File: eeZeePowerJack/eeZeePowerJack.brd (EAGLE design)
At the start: 29.2 x 13.7 mm, 10 parts, among them J1 POWER_JACKPTH, U2 LD29150DT

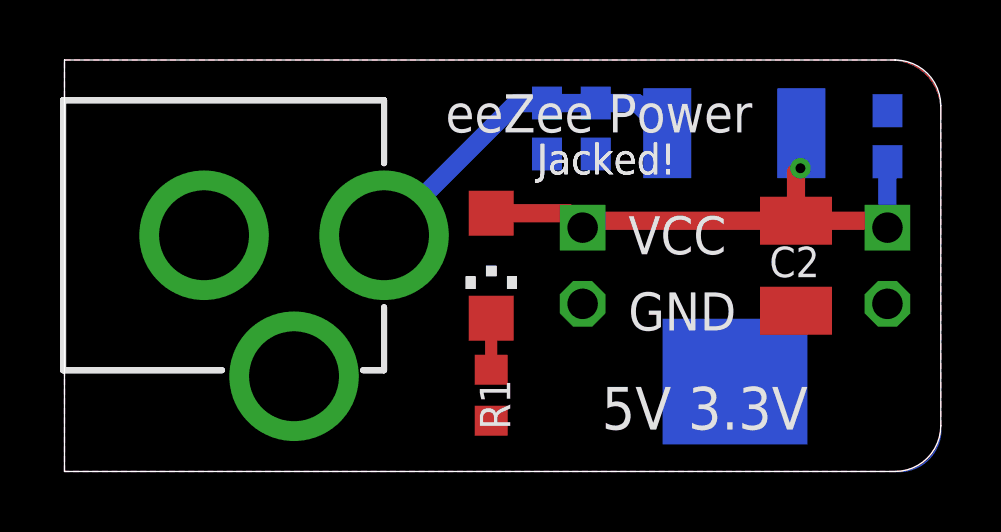
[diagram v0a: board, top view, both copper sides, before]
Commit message: Revised to use standard 1206 10uF part, moved bot thoughts silk.
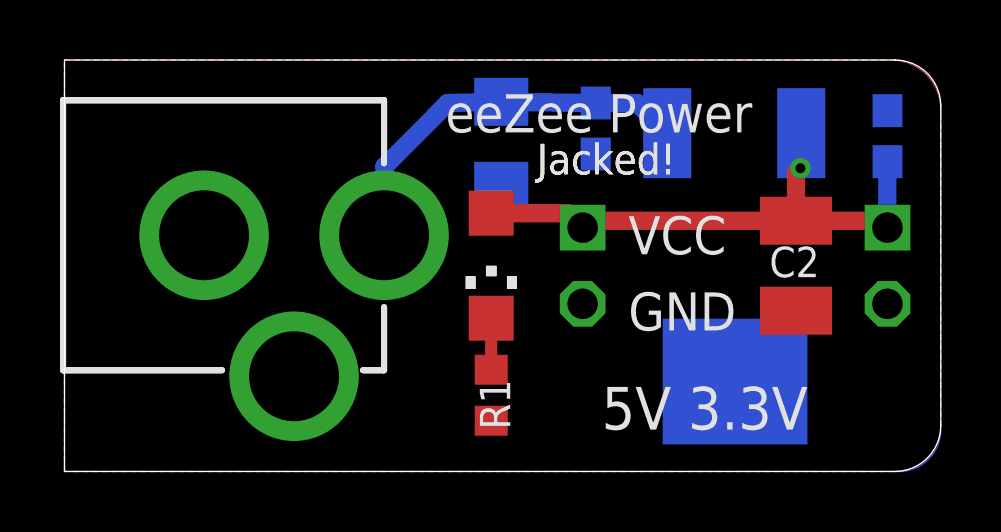
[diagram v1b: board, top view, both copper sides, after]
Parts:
- C3: device rcl:C0603 -> rcl:C1206
- J1: value POWER_JACKPTH -> POWER_JACK
- R1: value (none) -> 330
- moved C3 1.61 mm to (14.6, 10.9)
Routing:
- net VIN: track 11.7 -> 13.0 mm
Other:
- board text added: "Rev 0.2"
- board text removed: "Rev 0.1"
- board text removed: "U2"
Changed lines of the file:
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@@
 <layer number="18" name="Vias" color="2" fill="1" visible="yes" active="yes"/>
 <layer number="19" name="Unrouted" color="6" fill="1" visible="yes" active="yes"/>
-<layer number="20" name="Dimension" color="15" fill="1" visible="no" active="yes"/>
+<layer number="20" name="Dimension" color="15" fill="1" visible="yes" active="yes"/>
 <layer number="21" name="tPlace" color="7" fill="1" visible="no" active="yes"/>
-<layer number="22" name="bPlace" color="7" fill="1" visible="yes" active="yes"/>
+<layer number="22" name="bPlace" color="7" fill="1" visible="no" active="yes"/>
 <layer number="23" name="tOrigins" color="15" fill="1" visible="no" active="yes"/>
 <layer number="24" name="bOrigins" color="15" fill="1" visible="no" active="yes"/>
 <layer number="25" name="tNames" color="7" fill="1" visible="no" active="yes"/>
-<layer number="26" name="bNames" color="7" fill="1" visible="yes" active="yes"/>
+<layer number="26" name="bNames" color="7" fill="1" visible="no" active="yes"/>
 <layer number="27" name="tValues" color="7" fill="1" visible="no" active="yes"/>
 <layer number="28" name="bValues" color="7" fill="1" visible="no" active="yes"/>
@@
 <text x="17.907" y="1.389" size="1.4224" layer="27" font="vector">5V 3.3V</text>
 <text x="12.7" y="11.295" size="1.27" layer="27" font="vector">eeZee Power</text>
-<text x="13.843" y="1.516" size="0.8128" layer="22" font="vector" rot="MR90">bot-thoughts.com</text>
-<text x="4.572" y="12.311" size="1.27" layer="22" font="vector" rot="MR180">Rev 0.1</text>
+<text x="0.889" y="1.262" size="0.8128" layer="22" font="vector" rot="MR90">bot-thoughts.com</text>
+<text x="4.572" y="12.311" size="1.27" layer="22" font="vector" rot="MR180">Rev 0.2</text>
 <text x="18.796" y="7.231" size="1.27" layer="27" font="vector">VCC</text>
 <text x="18.796" y="4.691" size="1.27" layer="27" font="vector">GND</text>
 <text x="15.748" y="9.898" size="1.016" layer="25" font="vector">Jacked!</text>
-<wire x1="10.651996875" y1="3.366009375" x2="10.651996875" y2="5.46600625" width="0.2032" layer="121"/>
+<wire x1="10.651996875" y1="3.366009375" x2="10.651996875" y2="5.466003125" width="0.2032" layer="121"/>
 <wire x1="-0.04800625" y1="3.366009375" x2="5.252009375" y2="3.366009375" width="0.2032" layer="121"/>
 <wire x1="10.651996875" y1="3.366009375" x2="9.952" y2="3.366009375" width="0.2032" layer="121"/>
@@
 <wire x1="10.651996875" y1="12.365990625" x2="10.651996875" y2="10.26599375" width="0.2032" layer="121"/>
 <wire x1="-0.04800625" y1="12.365990625" x2="-0.04800625" y2="3.366009375" width="0.2032" layer="121"/>
-<rectangle x1="14.74899375" y1="6.07499375" x2="15.0740125" y2="6.4999875" layer="121" rot="R180"/>
-<rectangle x1="13.3739875" y1="6.07499375" x2="13.69900625" y2="6.4999875" layer="121" rot="R180"/>
-<rectangle x1="14.04899375" y1="6.4999875" x2="14.39900625" y2="6.85" layer="121" rot="R180"/>
-<text x="13.843" y="1.516" size="0.8128" layer="122" font="vector" ratio="25" rot="MR90">bot-thoughts.com</text>
-<text x="4.572" y="12.311" size="1.27" layer="122" font="vector" ratio="16" rot="MR180">Rev 0.1</text>
+<rectangle x1="14.74899375" y1="6.07499375" x2="15.0740125" y2="6.5000125" layer="121" rot="R180"/>
+<rectangle x1="13.3739875" y1="6.07499375" x2="13.69900625" y2="6.5000125" layer="121" rot="R180"/>
+<rectangle x1="14.04899375" y1="6.5000125" x2="14.39900625" y2="6.85" layer="121" rot="R180"/>
+<text x="0.889" y="1.262" size="0.8128" layer="122" font="vector" ratio="25" rot="MR90">bot-thoughts.com</text>
+<text x="4.572" y="12.311" size="1.27" layer="122" font="vector" ratio="16" rot="MR180">Rev 0.2</text>
 <wire x1="16.002" y1="8.755" x2="16.002" y2="7.485" width="0.2032" layer="122"/>
 <wire x1="16.002" y1="7.485" x2="16.637" y2="6.85" width="0.2032" layer="122"/>
@@
 <wire x1="25.5016" y1="9.3646" x2="19.1516" y2="9.3646" width="0.2032" layer="122"/>
 <text x="15.748" y="9.898" size="1.016" layer="121" font="vector" ratio="20">Jacked!</text>
-<text x="19.812" y="6.85" size="1.016" layer="122" font="vector" ratio="20" rot="MR180">U2</text>
 <text x="17.907" y="1.389" size="1.4224" layer="121" font="vector" ratio="15">5V 3.3V</text>
 <text x="12.7" y="11.295" size="1.27" layer="121" font="vector" ratio="16">eeZee Power</text>
@@
 <element name="C1" library="rcl" package="C0603" value="0.1uF" x="17.707" y="11.422" smashed="yes" rot="MR270">
 <attribute name="NAME" x="17.326" y="10.533" size="1.016" layer="26" font="vector" rot="MR90"/>
-<attribute name="VOLTAGE" value="10V" x="17.707" y="11.422" size="1.778" layer="28" rot="MR270" display="off"/>
+<attribute name="VOLTAGE" value="25V" x="17.707" y="11.422" size="1.778" layer="28" rot="MR270" display="off"/>
 </element>
 <element name="C2" library="rcl" package="SMC_B" value="100uF" x="24.384" y="6.85" smashed="yes" rot="R270">
 <attribute name="NAME" x="23.495" y="6.469" size="1.016" layer="25" font="vector"/>
 </element>
-<element name="R1" library="resistor" package="R0603" value="" x="14.224" y="2.532" smashed="yes" rot="R90">
+<element name="R1" library="resistor" package="R0603" value="330" x="14.224" y="2.532" smashed="yes" rot="R90">
 <attribute name="NAME" x="14.859" y="1.389" size="1.016" layer="25" font="vector" rot="R90"/>
-<attribute name="VALUE" x="16.256" y="1.643" size="1.27" layer="27" rot="R90"/>
-</element>
-<element name="C3" library="rcl" package="C0603" value="10uF" x="16.083" y="11.422" smashed="yes" rot="MR270">
-<attribute name="NAME" x="15.448" y="10.279" size="1.016" layer="26" font="vector" rot="MR90"/>
-<attribute name="VOLTAGE" value="10V" x="16.083" y="11.422" size="1.778" layer="28" rot="MR270" display="off"/>
+</element>
+<element name="C3" library="rcl" package="C1206" value="10uF" x="14.559" y="10.914" smashed="yes" rot="MR270">
+<attribute name="NAME" x="13.924" y="9.771" size="1.016" layer="26" font="vector" rot="MR90"/>
+<attribute name="VOLTAGE" value="25V" x="14.559" y="10.914" size="1.778" layer="28" rot="MR270" display="off"/>
 </element>
 <element name="C4" library="rcl" package="C0603" value="0.1uF" x="27.432" y="11.168" smashed="yes" rot="MR90">
@@
 <attribute name="VALUE" x="30.607" y="9.39" size="1.27" layer="28" rot="MR270"/>
 </element>
-<element name="J1" library="SparkFun-Connectors" package="POWER_JACK_PTH" value="POWER_JACKPTH" x="-3.048" y="7.866" smashed="yes" rot="R270"/>
+<element name="J1" library="SparkFun-Connectors" package="POWER_JACK_PTH" value="POWER_JACK" x="-3.048" y="7.866" smashed="yes" rot="R270"/>
 <element name="U2" library="bt_regulator" package="DPAK" value="LD29150DT" x="22.352" y="7.612" smashed="yes" rot="MR180">
 <attribute name="NAME" x="19.812" y="6.85" size="1.016" layer="26" font="vector" ratio="10" rot="MR180"/>
@@
 <contactref element="C1" pad="1"/>
 <contactref element="C3" pad="1"/>
-<wire x1="16.083" y1="12.272" x2="17.707" y2="12.272" width="0.6096" layer="16"/>
+<wire x1="14.559" y1="12.314" x2="17.707" y2="12.272" width="0.6096" layer="16"/>
 <contactref element="J1" pad="PWR"/>
 <contactref element="U2" pad="1"/>
 <wire x1="17.707" y1="12.272" x2="19.089" y2="12.272" width="0.6096" layer="16"/>
 <wire x1="19.089" y1="12.272" x2="20.0914" y2="11.2696" width="0.6096" layer="16"/>
-<wire x1="16.083" y1="12.272" x2="15.058" y2="12.272" width="0.6096" layer="16"/>
-<wire x1="15.058" y1="12.272" x2="10.652" y2="7.866" width="0.6096" layer="16"/>
+<wire x1="14.559" y1="12.314" x2="12.772" y2="12.272" width="0.6096" layer="16"/>
+<wire x1="12.772" y1="12.272" x2="10.668" y2="10.16" width="0.6096" layer="16"/>
+<wire x1="10.668" y1="10.16" x2="10.668" y2="7.866" width="0.6096" layer="16"/>
+<wire x1="10.668" y1="7.866" x2="10.652" y2="7.866" width="0.6096" layer="16"/>
 </signal>
 <signal name="GND">

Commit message: Replaced regulator with a lower cost one. Rearranged layout. Regulator on top (heat), capacitors on the bottom. Labeling rearranged.
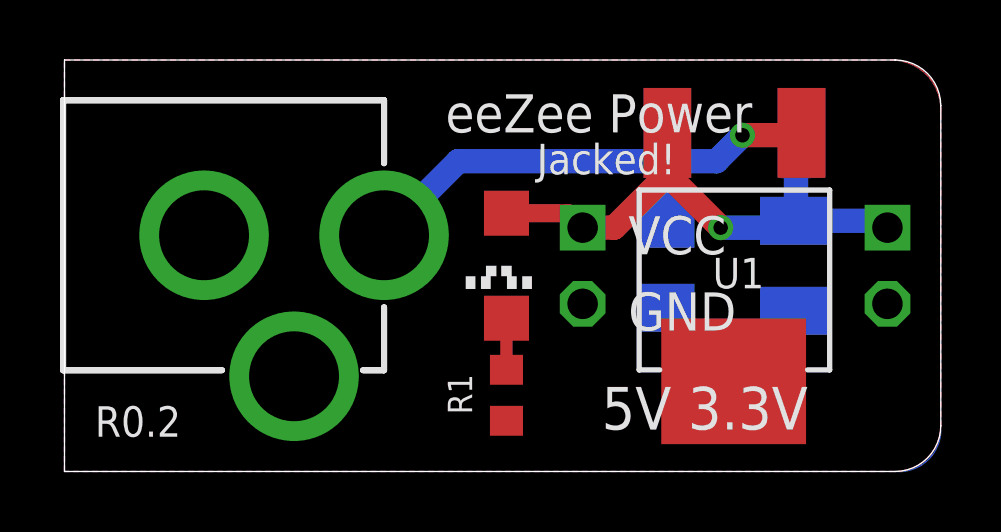
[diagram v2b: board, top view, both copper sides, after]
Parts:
- removed U2: LD29150DT, bt_regulator:DPAK
- added U1: LF50CDT, bt_regulator:DPAK
- moved C3 6.87 mm to (20.1, 6.85)
- moved C4 3.05 mm to (24.4, 11.2)
- moved C1 2.40 mm to (20.1, 11.2), turned to 90 degrees
- moved LED1 0.51 mm to (14.7, 6.85)
- moved R1 0.51 mm to (14.7, 2.53)
- flipped C2 to the bottom
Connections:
- net GND: now also U1.4; no longer U2.4
- net VIN: now also U1.1; no longer U2.1
- net VOUT: now also U1.3; no longer U2.3
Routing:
- net VIN: track 13.0 -> 17.8 mm, vias 0 -> 1
- net VOUT: track 18.8 -> 17.9 mm
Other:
- board text added: "3.3V"
- board text added: "5V"
- board text added: "R0.2"
